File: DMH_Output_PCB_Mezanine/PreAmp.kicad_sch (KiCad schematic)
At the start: 44 parts, among them J13 Conn_01x06, J28 Conn_01x06, J33 Conn_01x06, J35 Conn_01x02_PinHeader, J36 Conn_01x02_PinHeader, J39 Conn_01x02_PinHeader, J40 Conn_01x02_PinHeader, U16 NE5532, U17 NE5532, U18 NE5532, U19 NE5532

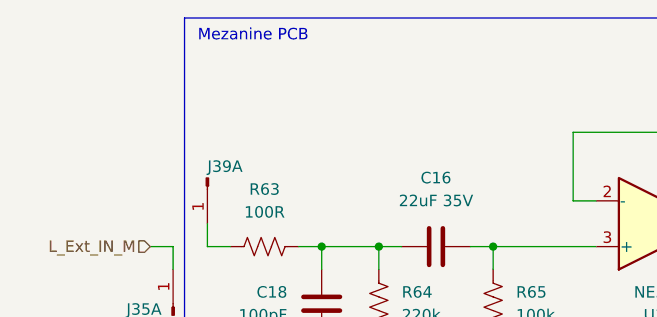
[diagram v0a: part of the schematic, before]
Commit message: Started Mezanine PCB project
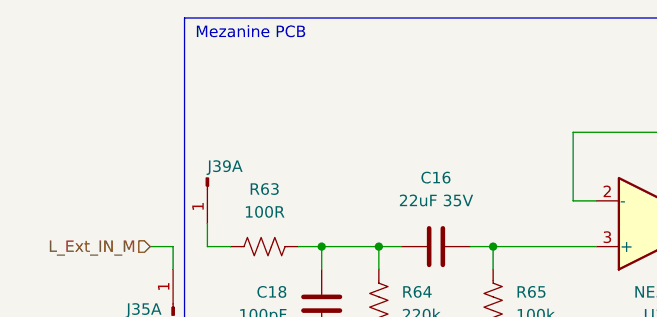
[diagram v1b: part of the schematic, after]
